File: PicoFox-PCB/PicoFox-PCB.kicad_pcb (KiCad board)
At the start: 4 copper layers, 40 x 58.5 mm, 143 parts, among them J2 Conn_01x03_Pin, J3 Conn_02x10_Counter_Clockwise, J4 Conn_Coaxial_Small, J5 USB-TYPE-C-018 (DEALON), Q1 AO3407A, SW3 SK-12D15-G030, U1 BVA1761, U15 USBLC6-2SC6, U16 BQ21040DBVR, U19 ME6217C33M5G, U2 W25Q128JVS, U3 RP2040, U4 Si5351A-B-GT, Y1 ABM8-272-T3, Y2 TG2016SMN_25.0000M-MCGNNM0

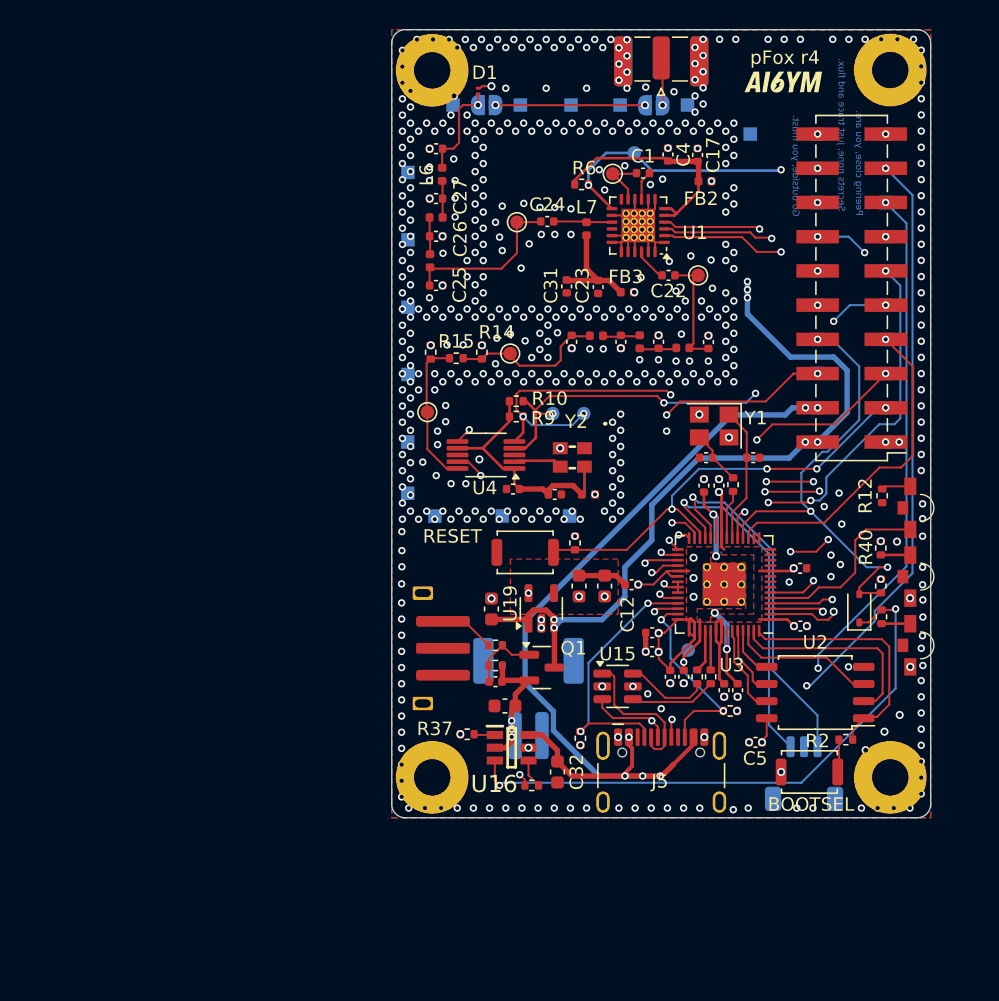
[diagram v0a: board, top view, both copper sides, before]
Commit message: Initial commit with SSTV support
This is the initial commit that supports SSTV, and file switching.

Includes first pass of the new badge-style fox for Pacificon - HAS NOT BEEN TESTED YET.

**** THIS CODE CONTAINS A LOT OF AI. PLEASE READ THE README.MD ****

Things changed/added to firmware:
- Add SSTV_ENABLE, SSTV_MODE, and VOICE_ENABLE settings
- Support SSTV-only and alternating voice/SSTV operation
- Decode 320x240 JPEGs directly from flash
- Cycle sstv.jpg, sstv1.jpg, sstv2.jpg, etc.
- Add Robot36 color Y/Cb/Cr encoding
- Use separate 5 kHz audio and 3 kHz SSTV FM deviation
- Optimize Si5351 modulation for 8 kHz / 125 us SSTV timing
- Precompute image color data, sine/PLL lookup tables, and phase increments
- Keep SSTV centered at zero carrier offset
- Protect flash access from USB MSC races
- Remove obsolete test-pattern and experimental timing code
- Add timing-critical code documentation
- Add v35 firmware version reporting to keep track of things for the AI side of the house.
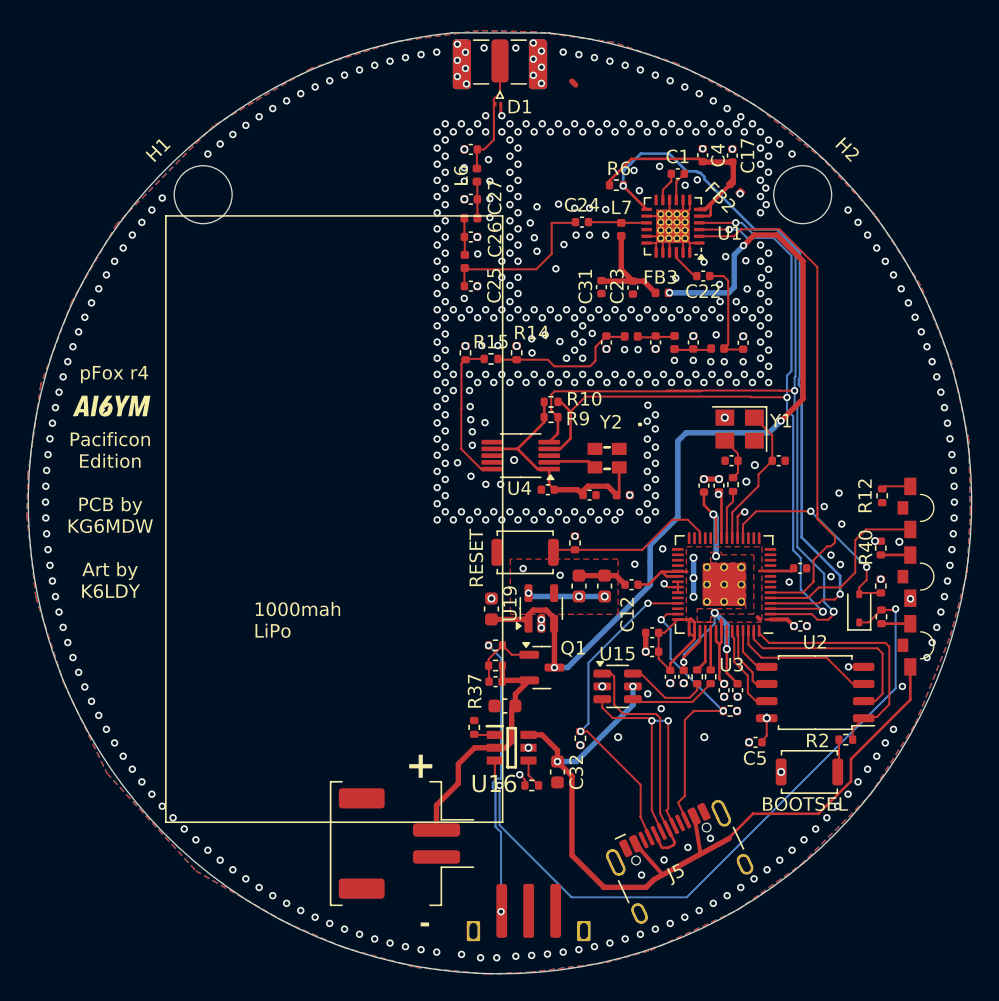
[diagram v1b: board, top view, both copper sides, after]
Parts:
- removed H3, H4: MountingHole, MountingHole:MountingHole_2.7mm_M2.5_Pad
- removed J2: Conn_01x03_Pin, Connector_JST:JST_SH_SM03B-SRSS-TB_1x03-1MP_P1.00mm_Horizontal
- removed J3: Conn_02x10_Counter_Clockwise, Connector_PinHeader_2.54mm:PinHeader_2x10_P2.54mm_Vertical_SMD
- removed JP1, JP2: SolderJumper_2_Open, Jumper:SolderJumper-2_P1.3mm_Open_RoundedPad1.0x1.5mm
- removed TP1, TP2, TP3, TP4, TP5, TP6, TP7, TP8, TP9: TestPoint, TestPoint:TestPoint_Pad_D1.0mm
- removed TP14, TP17, TP19, TP20, TP21, TP22, TP23, TP24, TP25, TP26, TP27, TP28, TP29, TP30, TP31, TP32, TP33, TP34, TP35, TP36, TP37, TP38, TP39, TP40, TP41, TP42, TP43, TP44, TP45, TP46, TP47, TP48, TP49, TP51, TP53: TestPoint, PicofoxLib:Castellation Pad
- added G***: LOGO, PicofoxLib:IAMTHEFOX_Logo_ExtraPoints, B.Cu at (58.0, 88.6)
- BT2: moved to F.Cu
- H1, H2: value MountingHole -> Lanyard Hole; footprint MountingHole:MountingHole_2.7mm_M2.5_Pad -> MountingHole:MountingHole_4.3mm_M4_DIN965
- moved G*** 55.3 mm to (29.2, 81.4)
- moved SW3 22.4 mm to (60.2, 120.4), turned to 0 degrees
- moved H1 19.3 mm to (36.0, 65.8), turned to 45 degrees
- moved J4 12.0 mm to (58.0, 55.8)
- moved H2 11.3 mm to (80.5, 65.8), turned to -45 degrees
- moved BT2 10.5 mm to (53.3, 113.9), turned to 90 degrees
- moved J5 6.80 mm to (71.7, 116.0), turned to 25 degrees
- moved C24 2.58 mm to (64.1, 67.8)
- moved C31 2.58 mm to (65.6, 72.6)
- moved C1 2.58 mm to (71.2, 64.2)
- moved C17 2.58 mm to (75.3, 62.9)
- moved C18 2.58 mm to (65.9, 76.7)
- moved C19 2.58 mm to (69.6, 76.7)
- moved C20 2.58 mm to (72.4, 76.7)
- moved C21 2.58 mm to (76.1, 76.7)
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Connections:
- J4 pad 1: Net-(J4-In) -> Net-(D1-A2)
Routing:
- net /GPIO20: track 66.7 -> 0.00 mm, vias 2 -> 0
- net /GPIO21: track 64.7 -> 0.00 mm, vias 3 -> 0
- net /GPIO28_ADC2: track 58.0 -> 0.00 mm, vias 3 -> 0
- net /GPIO26_ADC0: track 53.4 -> 0.00 mm, vias 3 -> 0
- net /CC2Sense: track 69.6 -> 19.6 mm, vias 3 -> 2
- net /CC1Sense: track 71.7 -> 22.3 mm, vias 3 -> 2
- net VBUS: track 92.7 -> 48.0 mm, vias 8 -> 2
- net /CLK1: track 39.5 -> 0.00 mm, vias 3 -> 0
- net /GPIO19: track 36.9 -> 0.00 mm, vias 4 -> 0
- net /GPIO18: track 35.2 -> 0.00 mm, vias 4 -> 0
- net /GPIO16: track 31.1 -> 0.00 mm, vias 5 -> 0
- net /CLK2: track 29.6 -> 0.00 mm, vias 3 -> 0
- net /GPIO17: track 28.5 -> 0.00 mm, vias 4 -> 0
- net /SWCLK: track 27.1 -> 0.00 mm, vias 1 -> 0
- net /SWD: track 26.2 -> 0.00 mm, vias 1 -> 0
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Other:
- board size 40 x 58.5 mm -> 70 x 69.8 mm
- board text added: "+"
- board text added: "-"
- board text added: "1000mah LiPo"
- board text added: "Pacificon Edition PCB by KG6MDW Art by K6LDY"
- board text removed: "+ -"
- board text removed: "1.1V"
- board text removed: "AMP_EN"
- board text removed: "Go outside, you must."
- board text removed: "Peering close, you are."
- board text removed: "SDA SCL"
- board text removed: "SWD"
- board text removed: "Secrets none, just trace and flux."

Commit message: Minor updates
Adding AI6YM firmware with fix for forced format of filesystem. Updated PCB/Gerbers.
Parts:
- G***: moved to F.Cu
- G***: footprint PicofoxLib:IAMTHEFOX_Logo_ExtraPoints -> PicofoxLib:IAMTHEFOX_Logo
- moved G*** 27.4 mm to (37.2, 81.2), turned to 0 degrees
